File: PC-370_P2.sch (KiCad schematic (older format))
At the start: 85 parts, among them J1 PC/370-P-M Cable, J2 Bus_ISA_16bit, U1 Conn_02x20_Counter_Clockwise, U10 74LS112, U11 74LS138, U12 74LS138, U13 74S74, U15 74LS20, U16 74LS10, U17 74S00, U18 74S00, U19 74LS175, U2 74LS245, U20 74LS175, U21 74S51, U22 74LS51, U23 74S00, U24 74LS32, U25 74LS245, U26 74LS374, U27 74LS373, U28 74LS374, U29 74LS374, U3 74LS374, U30 74LS244, U31 74S86, U32 74LS20, U33 74LS04, U34 74LS02, U35 74S00, U36 74S74, U37 74S74, U38 74S10, U39 74LS10, U4 74LS374, U40 74S00, U41 74LS02, U42 74LS138, U43 74LS32, U44 74LS153, U45 74LS157, U46 74LS153, U47 74LS153, U48 74S30, U49 74LS00, U5 74LS374, U50 74LS08, U51 74LS30, U52 74LS10, U53 74S09, U54 74LS112, U55 74LS27, U56 IBM_R_Network13_US, U57 74LS04, U58 74LS112, U59 74LS27, U6 74LS245, U60 74LS20, U61 74LS157, U62 74LS244, U63 74LS153, U64 74S157, U66 68000-PGA, U67 68000-PGA, U68 SY2128-1, U69 SY2128-1, U7 74S280, U70 74S241, U71 74LS32, U72 74LS74, U73 74S112, U74 74S112, U75 74LS02, U76 74LS138, U77 74LS125, U78 74LS175, U79 74LS367, U8 74LS02, U80 74LS175, U81 74LS244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

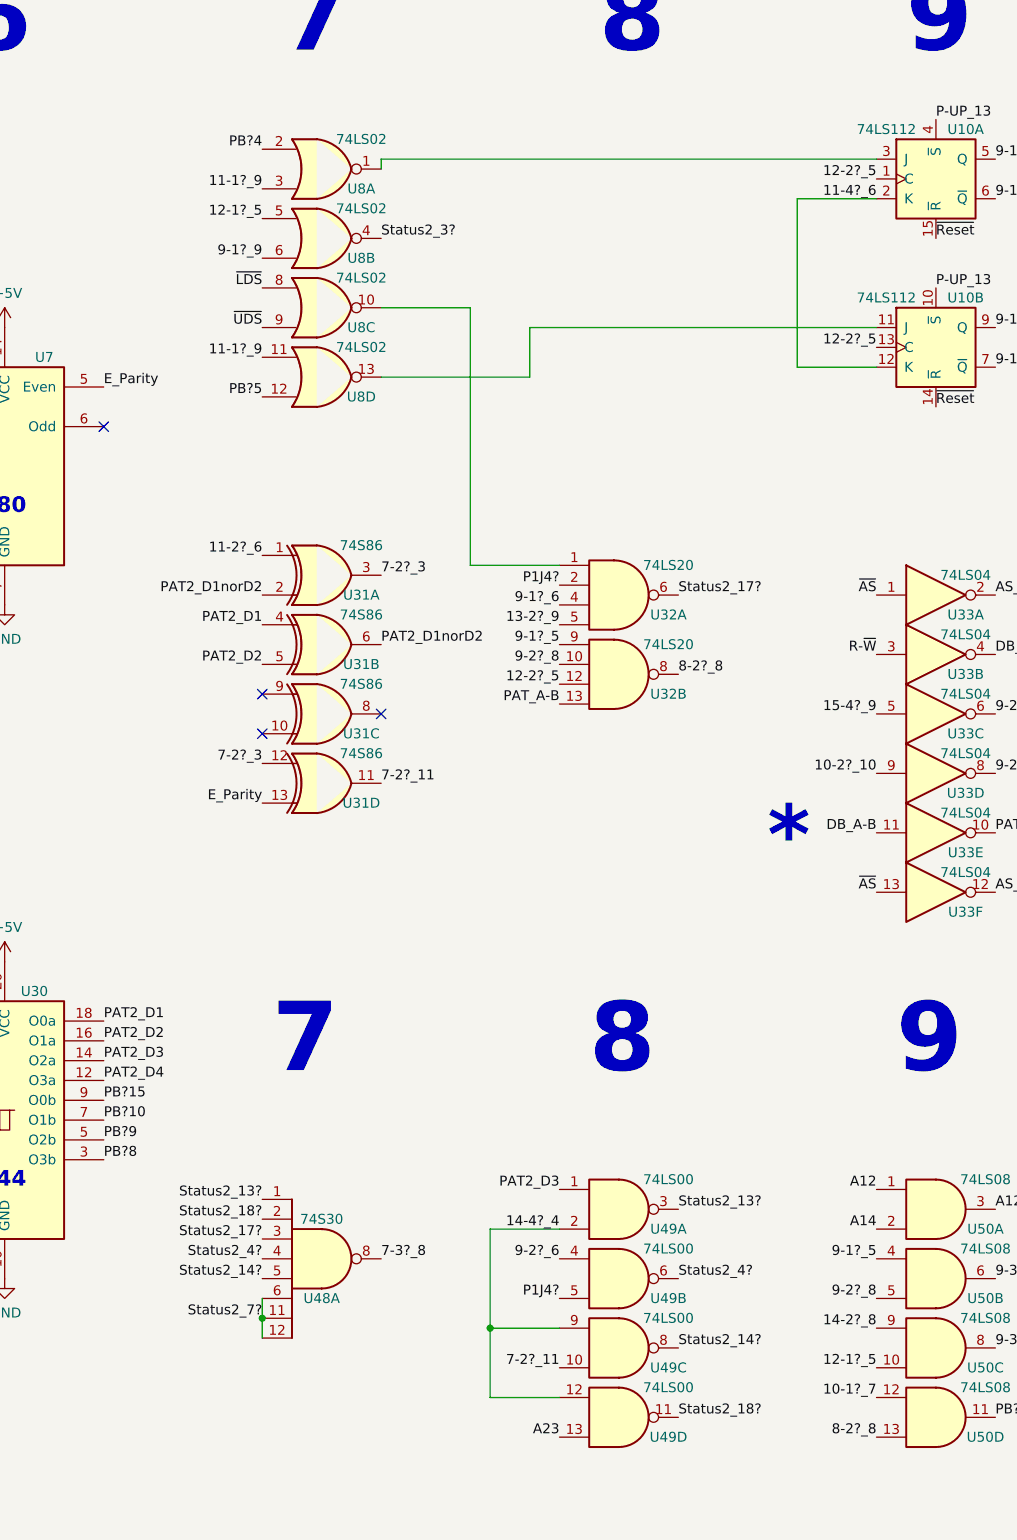
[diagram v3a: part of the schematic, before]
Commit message: Some clean-up and net name correction.
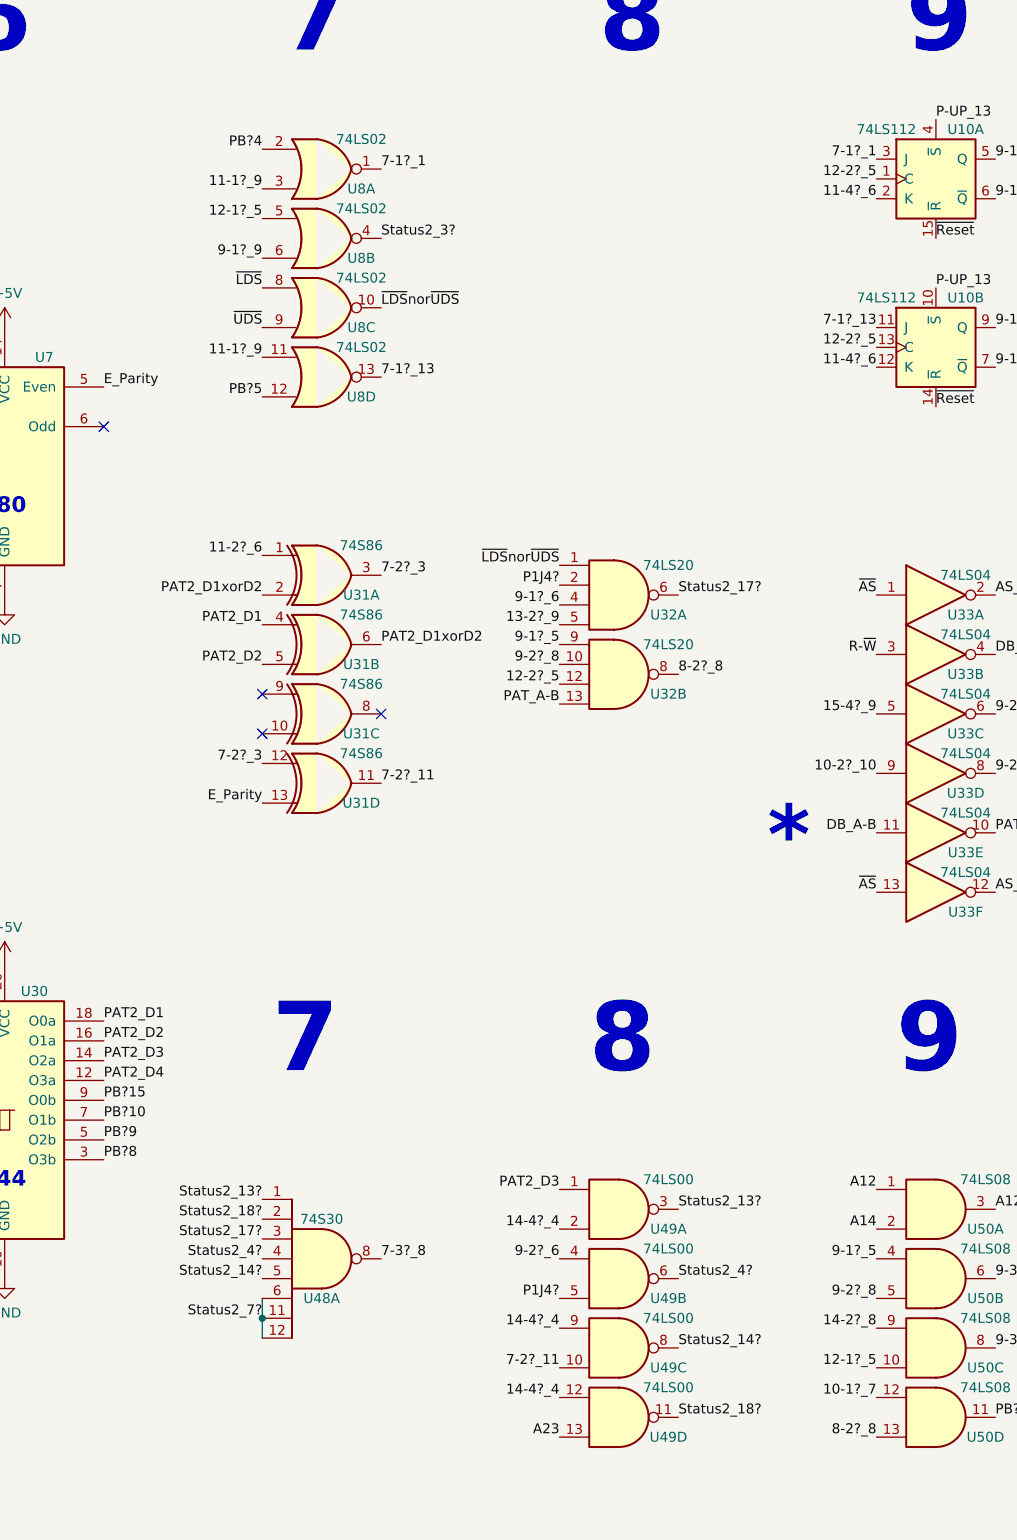
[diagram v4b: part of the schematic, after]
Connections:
- net ~LDS~nor~UDS: now reaches U32.1, U8.10
- net 7-1?_1: now reaches U10.3 (J), U8.1
- net 7-1?_13: now reaches U10.11 (J), U8.13
- net PAT2_D1norD2 renamed PAT2_D1xorD2
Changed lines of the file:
@@
 E_Parity
 NoConn ~ 11500 13450
-Wire Wire Line
-	15400 12100 12900 12100
-Wire Wire Line
-	12900 12100 12900 12150
 Text Label 19650 12900 0    50   ~ 0
 11-1?_9
@@
 Text Label 12300 12600 2    50   ~ 0
 9-1?_9
-Wire Wire Line
-	12900 12850 13350 12850
-Wire Wire Line
-	13350 12850 13350 14150
-Wire Wire Line
-	13350 14150 13800 14150
-Wire Wire Line
-	12900 13200 13650 13200
-Wire Wire Line
-	13650 13200 13650 12950
-Wire Wire Line
-	13650 12950 15400 12950
 Text Label 19450 14700 0    50   ~ 0
 11-2?_6
@@
 Text Label 35750 12050 2    50   ~ 0
 12-2?_5
-Wire Wire Line
-	13800 17500 13450 17500
-Wire Wire Line
-	13450 17500 13450 18000
-Wire Wire Line
-	13450 18000 13800 18000
-Wire Wire Line
-	13450 18000 13450 18350
-Wire Wire Line
-	13450 18350 13800 18350
-Connection ~ 13450 18000
 Text Label 25150 20200 0    50   ~ 0
 14-4?_4
@@
 Text Label 13800 18550 2    50   ~ 0
 A23
-Wire Wire Line
-	15400 12300 15000 12300
-Wire Wire Line
-	15000 12300 15000 13150
-Wire Wire Line
-	15000 13150 15400 13150
 Text Label 19450 20050 0    50   ~ 0
 11-4?_6
@@
 	22500 20350 22500 20050
 Text Label 12900 14550 0    50   ~ 0
-PAT2_D1norD2
+PAT2_D1xorD2
 Text Label 12300 14300 2    50   ~ 0
-PAT2_D1norD2
+PAT2_D1xorD2
 Text Label 12900 14200 0    50   ~ 0
 7-2?_3
@@
 Text Notes 22400 19500 0    79   ~ 16
 Clock Divider
+Text Label 13800 18000 2    50   ~ 0
+14-4?_4
+Text Label 13800 18350 2    50   ~ 0
+14-4?_4
+Text Label 12900 12850 0    50   ~ 0
+~LDS~nor~UDS
+Text Label 13800 14150 2    50   ~ 0
+~LDS~nor~UDS
+Text Label 15400 13150 2    50   ~ 0
+11-4?_6
+Text Label 12900 12150 0    50   ~ 0
+7-1?_1
+Text Label 15400 12100 2    50   ~ 0
+7-1?_1
+Text Label 12900 13200 0    50   ~ 0
+7-1?_13
+Text Label 15400 12950 2    50   ~ 0
+7-1?_13
 $EndSCHEMATC
